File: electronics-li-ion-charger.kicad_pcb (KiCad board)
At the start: 2 copper layers, 16 parts, among them J1 Conn_01x01_Male, J2 Conn_01x01_Male, J3 USB_B_Micro, J4 Conn_01x03_Male, U1 MCP73831-2-OT

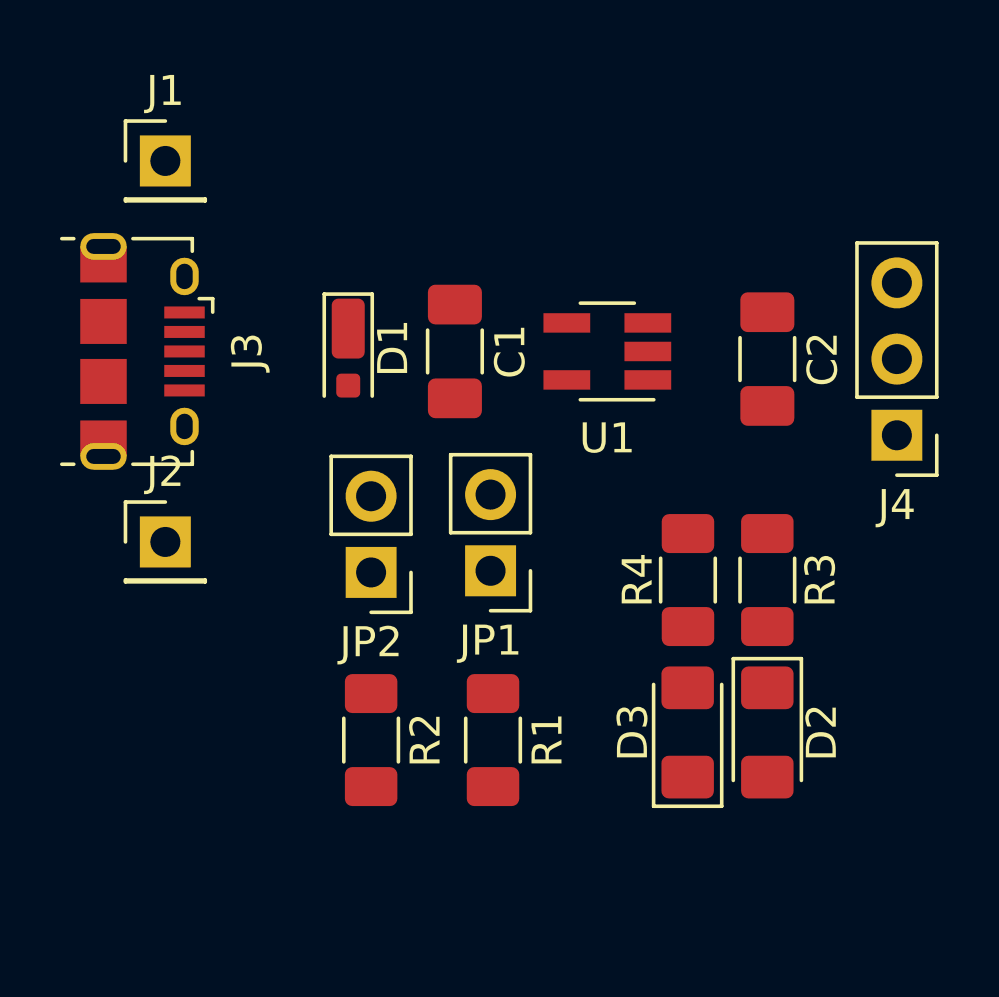
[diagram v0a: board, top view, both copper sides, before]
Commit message: Place components in PCB layout.
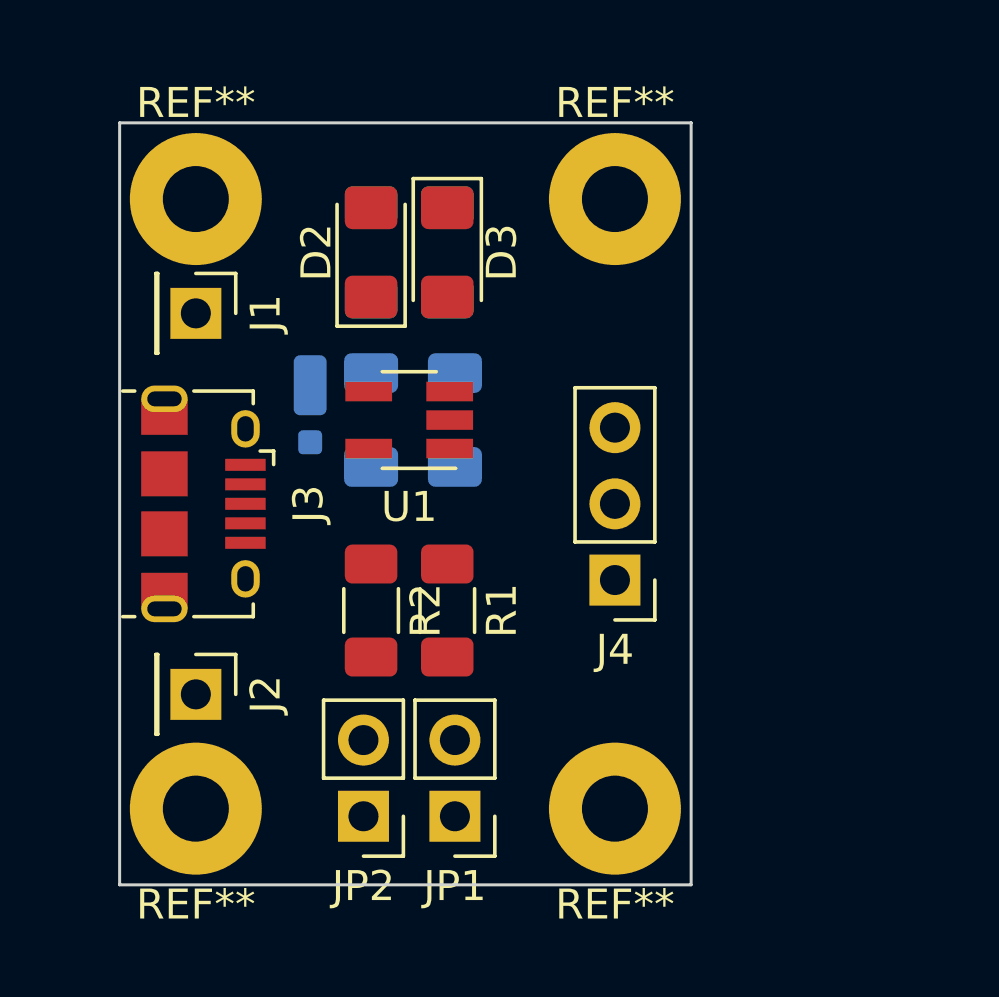
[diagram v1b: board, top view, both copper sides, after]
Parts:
- added REF**: MountingHole_2.2mm_M2_Pad, MountingHole:MountingHole_2.2mm_M2_Pad, F.Cu at (143.5, 91.4)
- added REF**: MountingHole_2.2mm_M2_Pad, MountingHole:MountingHole_2.2mm_M2_Pad, F.Cu at (143.5, 111.8)
- added REF**: MountingHole_2.2mm_M2_Pad, MountingHole:MountingHole_2.2mm_M2_Pad, F.Cu at (129.5, 111.8)
- added REF**: MountingHole_2.2mm_M2_Pad, MountingHole:MountingHole_2.2mm_M2_Pad, F.Cu at (129.5, 91.4)
- C1, C2, D1, R3, R4: moved to B.Cu
- moved D2 20.7 mm to (135.4, 93.2), turned to 90 degrees
- moved D3 17.9 mm to (137.9, 93.2), turned to 270 degrees
- moved R3 17.1 mm to (135.4, 93.2)
- moved R4 13.6 mm to (137.9, 93.2)
- moved C2 10.6 mm to (138.2, 98.8)
- moved J4 10.6 mm to (143.5, 104.1)
- moved JP1 8.27 mm to (138.2, 112.0)
- moved JP2 8.13 mm to (135.1, 112.0)
- moved U1 6.99 mm to (136.7, 98.8)
- moved J3 5.47 mm to (129.8, 101.6)
- moved J1 5.18 mm to (129.5, 95.2), turned to 270 degrees
- moved J2 5.18 mm to (129.5, 108.0), turned to 270 degrees
- moved R1 4.58 mm to (137.9, 105.2)
- moved R2 4.32 mm to (135.4, 105.2)
- moved C1 3.61 mm to (135.4, 98.8)
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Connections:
- D2 pad 1: Net-(D2-Pad1) -> STAT
- D2 pad 2: +5V -> Net-(D2-Pad2)
- D3 pad 1: GND -> Net-(D3-Pad1)
- D3 pad 2: Net-(D3-Pad2) -> STAT
- JP1 pad 1: Net-(JP1-Pad1) -> GND
- JP1 pad 2: PROG -> Net-(JP1-Pad2)
- JP2 pad 1: Net-(JP2-Pad1) -> GND
- JP2 pad 2: PROG -> Net-(JP2-Pad2)
- R1 pad 1: Net-(JP1-Pad1) -> PROG
- R1 pad 2: GND -> Net-(JP1-Pad2)
- R2 pad 1: Net-(JP2-Pad1) -> PROG
- R2 pad 2: GND -> Net-(JP2-Pad2)
- R3 pad 1: Net-(D2-Pad1) -> +5V
- R3 pad 2: STAT -> Net-(D2-Pad2)
- R4 pad 1: STAT -> Net-(D3-Pad1)
- R4 pad 2: Net-(D3-Pad2) -> GND
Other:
- board outline added: 19.1 x 25.4 mm

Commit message: Add traces to PCB layout.
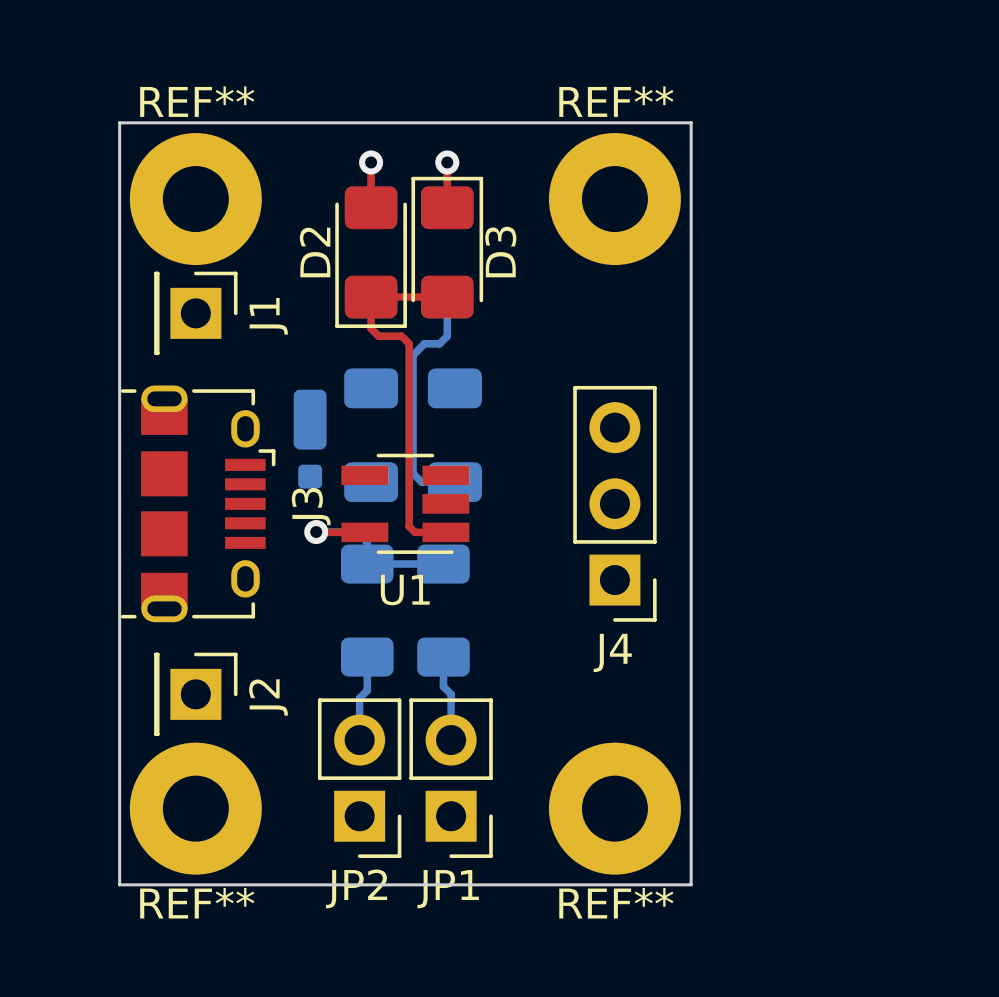
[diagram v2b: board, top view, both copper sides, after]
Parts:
- R1, R2: moved to B.Cu
- moved U1 2.80 mm to (136.5, 101.6)
- moved D1 1.14 mm to (133.3, 99.4)
- moved C1 0.51 mm to (135.4, 99.3)
- moved C2 0.51 mm to (138.2, 99.3)
- moved R1 0.13 mm to (137.8, 105.2)
- moved R2 0.13 mm to (135.3, 105.2)
- moved JP1 0.13 mm to (138.0, 112.0)
- moved JP2 0.13 mm to (135.0, 112.0)
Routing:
- net STAT: track 0.00 -> 12.5 mm
- net GND: track 0.00 -> 8.11 mm
- net PROG: track 0.00 -> 6.83 mm, vias 0 -> 1
- net Net-(D3-Pad1): track 0.00 -> 3.11 mm, vias 0 -> 1
- net Net-(D2-Pad2): track 0.00 -> 2.96 mm, vias 0 -> 1
- net Net-(JP1-Pad2): track 0.00 -> 2.87 mm
- net Net-(JP2-Pad2): track 0.00 -> 2.87 mm

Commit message: Add power planes.
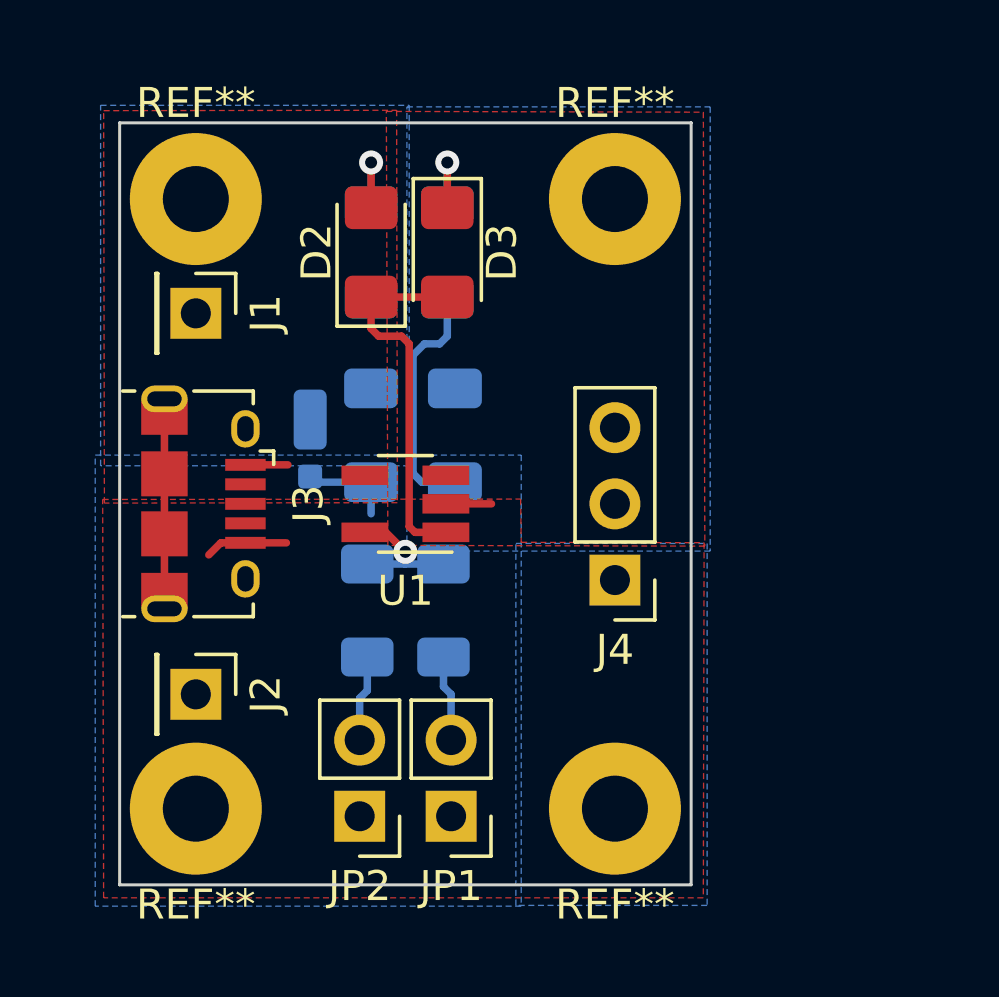
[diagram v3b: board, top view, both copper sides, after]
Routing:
- net GND: track 8.11 -> 15.5 mm
- net Net-(J3-Pad6): track 0.00 -> 5.80 mm
- net PROG: track 6.83 -> 5.34 mm
- net +5V: track 0.00 -> 1.41 mm
- added copper zone on B.Cu, net +5V
- added copper zone on F.Cu, net +5V
- added copper zone on B.Cu, net /VBAT
- added copper zone on F.Cu, net /VBAT
- added copper zone on B.Cu, net GND
- added copper zone on F.Cu, net GND
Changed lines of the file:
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@@
     (thickness 1.6)
     (drawings 4)
-    (tracks 35)
+    (tracks 45)
     (zones 0)
     (modules 20)
@@
     (trace_clearance 0.2)
     (zone_clearance 0.508)
-    (zone_45_only no)
+    (zone_45_only yes)
     (trace_min 0.2)
     (via_size 0.8)
@@
     (mod_text_size 1 1)
     (mod_text_width 0.15)
-    (pad_size 1.524 1.524)
-    (pad_drill 0.762)
+    (pad_size 1.56 0.65)
+    (pad_drill 0)
     (pad_to_mask_clearance 0)
     (aux_axis_origin 0 0)
@@
       (net 8 PROG))
     (pad 4 smd rect (at 1.35 0.95 180) (size 1.56 0.65) (layers F.Cu F.Paste F.Mask)
-      (net 2 +5V))
+      (net 2 +5V) (zone_connect 2))
     (pad 3 smd rect (at -1.35 0.95 180) (size 1.56 0.65) (layers F.Cu F.Paste F.Mask)
-      (net 9 /VBAT))
+      (net 9 /VBAT) (zone_connect 2))
     (pad 2 smd rect (at -1.35 0 180) (size 1.56 0.65) (layers F.Cu F.Paste F.Mask)
-      (net 1 GND))
+      (net 1 GND) (zone_connect 2))
     (pad 1 smd rect (at -1.35 -0.95 180) (size 1.56 0.65) (layers F.Cu F.Paste F.Mask)
       (net 3 STAT))
@@
   (segment (start 137.0715 100.8765) (end 138.176 100.8765) (width 0.25) (layer B.Cu) (net 1))
   (segment (start 136.779 100.584) (end 137.0715 100.8765) (width 0.25) (layer B.Cu) (net 1))
+  (segment (start 137.875 101.6) (end 139.3952 101.6) (width 0.25) (layer F.Cu) (net 1))
+  (segment (start 133.5355 100.8765) (end 133.35 100.691) (width 0.25) (layer B.Cu) (net 1))
+  (segment (start 135.382 100.8765) (end 133.5355 100.8765) (width 0.25) (layer B.Cu) (net 1))
+  (segment (start 135.382 100.8765) (end 135.382 101.9302) (width 0.25) (layer B.Cu) (net 1))
+  (segment (start 131.194 102.9) (end 130.3736 102.9) (width 0.25) (layer F.Cu) (net 1))
+  (segment (start 130.3736 102.9) (end 129.9718 103.3018) (width 0.25) (layer F.Cu) (net 1))
+  (segment (start 131.194 102.9) (end 132.558 102.9) (width 0.25) (layer F.Cu) (net 1))
+  (segment (start 131.194 100.3) (end 132.6088 100.3) (width 0.25) (layer F.Cu) (net 2))
   (segment (start 137.922 94.7055) (end 135.382 94.7055) (width 0.25) (layer F.Cu) (net 3))
   (segment (start 136.845 102.55) (end 137.875 102.55) (width 0.25) (layer F.Cu) (net 3))
@@
   (segment (start 135.382 95.758) (end 135.636 96.012) (width 0.25) (layer F.Cu) (net 3))
   (segment (start 135.382 94.7055) (end 135.382 95.758) (width 0.25) (layer F.Cu) (net 3))
+  (segment (start 128.494 98.7) (end 128.494 104.5) (width 0.25) (layer F.Cu) (net 4))
   (segment (start 135.3185 103.5425) (end 135.255 103.606) (width 0.25) (layer B.Cu) (net 8))
-  (segment (start 135.255 103.606) (end 137.795 103.606) (width 0.25) (layer B.Cu) (net 8))
-  (via (at 133.5532 102.5398) (size 0.8) (drill 0.4) (layers F.Cu B.Cu) (net 8))
-  (segment (start 133.5634 102.55) (end 133.5532 102.5398) (width 0.25) (layer F.Cu) (net 8))
-  (segment (start 135.175 102.55) (end 133.5634 102.55) (width 0.25) (layer F.Cu) (net 8))
-  (segment (start 133.5532 102.5398) (end 134.9248 102.5398) (width 0.25) (layer B.Cu) (net 8))
-  (segment (start 135.255 102.87) (end 135.255 103.606) (width 0.25) (layer B.Cu) (net 8))
-  (segment (start 134.9248 102.5398) (end 135.255 102.87) (width 0.25) (layer B.Cu) (net 8))
+  (segment (start 135.175 102.55) (end 135.860556 102.55) (width 0.25) (layer F.Cu) (net 8))
+  (via (at 136.523228 103.199683) (size 0.8) (drill 0.4) (layers F.Cu B.Cu) (net 8))
+  (segment (start 135.873545 102.55) (end 136.523228 103.199683) (width 0.25) (layer F.Cu) (net 8))
+  (segment (start 135.175 102.55) (end 135.873545 102.55) (width 0.25) (layer F.Cu) (net 8))
+  (segment (start 136.5117 103.211211) (end 136.5117 103.606) (width 0.25) (layer B.Cu) (net 8))
+  (segment (start 136.523228 103.199683) (end 136.5117 103.211211) (width 0.25) (layer B.Cu) (net 8))
+  (segment (start 136.5117 103.606) (end 137.795 103.606) (width 0.25) (layer B.Cu) (net 8))
+  (segment (start 135.255 103.606) (end 136.5117 103.606) (width 0.25) (layer B.Cu) (net 8))
   (segment (start 135.382 91.7305) (end 135.382 90.2208) (width 0.25) (layer F.Cu) (net 10))
   (segment (start 135.382 90.2208) (end 135.382 91.668) (width 0.25) (layer B.Cu) (net 10))
@@
   (segment (start 135.001 108.077) (end 135.001 109.474) (width 0.25) (layer B.Cu) (net 13))
   (segment (start 135.255 107.823) (end 135.001 108.077) (width 0.25) (layer B.Cu) (net 13))
+  (zone (net 1) (net_name GND) (layer F.Cu) (hatch edge 0.508)
+    (priority 2)
+    (connect_pads (clearance 0.508))
+    (min_thickness 0.254)
+    (fill yes (arc_segments 32) (thermal_gap 0.508) (thermal_bridge_width 0.508))
+    (polygon
+      (pts
+        (xy 146.4564 114.7318) (xy 126.4666 114.7318) (xy 126.43485 101.45395) (xy 140.36675 101.44125) (xy 140.3858 102.8827)
+        (xy 146.4818 102.8954)
+      )
+    )
+  )
+  (zone (net 2) (net_name +5V) (layer F.Cu) (hatch edge 0.508)
+    (priority 1)
+    (connect_pads (clearance 0.508))
+    (min_thickness 0.254)
+    (fill yes (arc_segments 32) (thermal_gap 0.508) (thermal_bridge_width 0.508))
+    (polygon
+      (pts
+        (xy 136.2583 101.5619) (xy 126.492 101.5746) (xy 126.4666 88.4936) (xy 136.2329 88.4809)
+      )
+    )
+  )
+  (zone (net 9) (net_name /VBAT) (layer F.Cu) (hatch edge 0.508)
+    (connect_pads (clearance 0.508))
+    (min_thickness 0.254)
+    (fill yes (arc_segments 32) (thermal_gap 0.508) (thermal_bridge_width 0.508))
+    (polygon
+      (pts
+        (xy 146.5072 103.0097) (xy 135.9408 102.9843) (xy 135.89 88.519) (xy 146.4564 88.5444)
+      )
+    )
+  )
+  (zone (net 1) (net_name GND) (layer B.Cu) (hatch edge 0.508)
+    (priority 2)
+    (connect_pads (clearance 0.508))
+    (min_thickness 0.254)
+    (fill yes (arc_segments 32) (thermal_gap 0.508) (thermal_bridge_width 0.508))
+    (polygon
+      (pts
+        (xy 140.3858 115.0112) (xy 126.1872 115.0112) (xy 126.1872 99.9744) (xy 140.3858 99.9744)
+      )
+    )
+  )
+  (zone (net 1) (net_name GND) (layer B.Cu) (hatch edge 0.508)
+    (priority 2)
+    (connect_pads (clearance 0.508))
+    (min_thickness 0.254)
+    (fill yes (arc_segments 32) (thermal_gap 0.508) (thermal_bridge_width 0.508))
+    (polygon
+      (pts
+        (xy 146.5834 114.9858) (xy 140.208 114.9858) (xy 140.208 102.9208) (xy 146.5834 102.9208)
+      )
+    )
+  )
+  (zone (net 2) (net_name +5V) (layer B.Cu) (hatch edge 0.508)
+    (priority 1)
+    (connect_pads (clearance 0.508))
+    (min_thickness 0.254)
+    (fill yes (arc_segments 32) (thermal_gap 0.508) (thermal_bridge_width 0.508))
+    (polygon
+      (pts
+        (xy 136.652 100.33) (xy 126.365 100.33) (xy 126.365 88.3158) (xy 136.652 88.3158)
+      )
+    )
+  )
+  (zone (net 9) (net_name /VBAT) (layer B.Cu) (hatch edge 0.508)
+    (connect_pads (clearance 0.508))
+    (min_thickness 0.254)
+    (fill yes (arc_segments 32) (thermal_gap 0.508) (thermal_bridge_width 0.508))
+    (polygon
+      (pts
+        (xy 146.685 103.1748) (xy 136.5758 103.1748) (xy 136.5758 88.3666) (xy 146.685 88.3666)
+      )
+    )
+  )
 )
